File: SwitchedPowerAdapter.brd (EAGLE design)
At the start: 27.6 x 12.9 mm, 8 parts, among them J1 CONN_42.54_SCREW, J2 CONN_42.54_SCREW

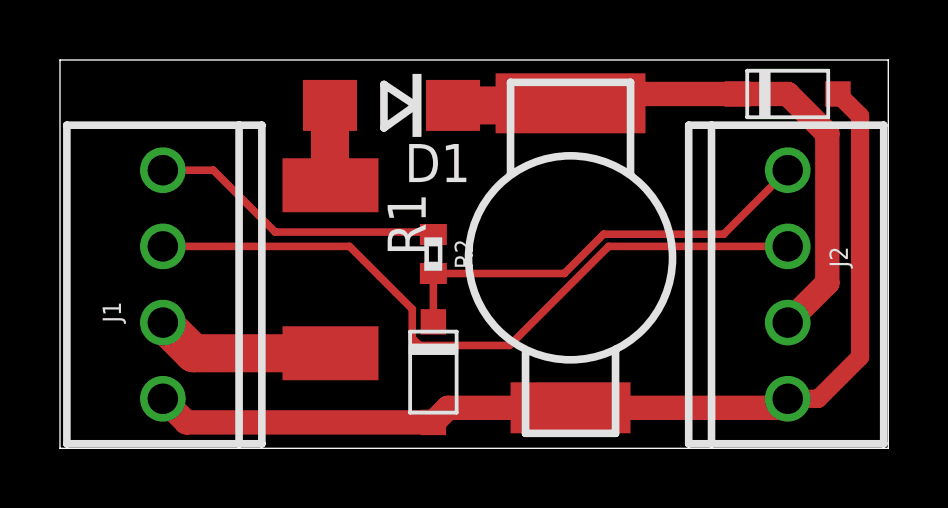
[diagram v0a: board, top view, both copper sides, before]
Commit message: Generated gerbers, updated part number on Switched Power
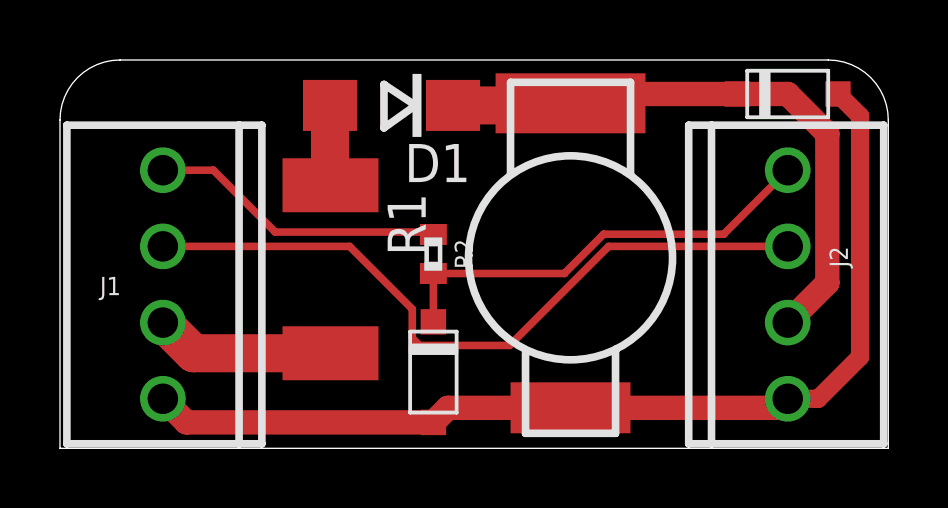
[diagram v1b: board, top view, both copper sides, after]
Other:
- outline, holes or cut-outs redrawn
- board text added: "Clk"
- board text added: "Data"
- board text added: "GND"
- board text added: "Tally Const Power"
- board text added: "To Logger"
- board text added: "To Tally"
- board text added: "VCap"
- board text added: "Vin"
